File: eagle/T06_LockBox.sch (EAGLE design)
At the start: 28 parts, among them T1 2N3904, T2 2N3904, T3 2N3904

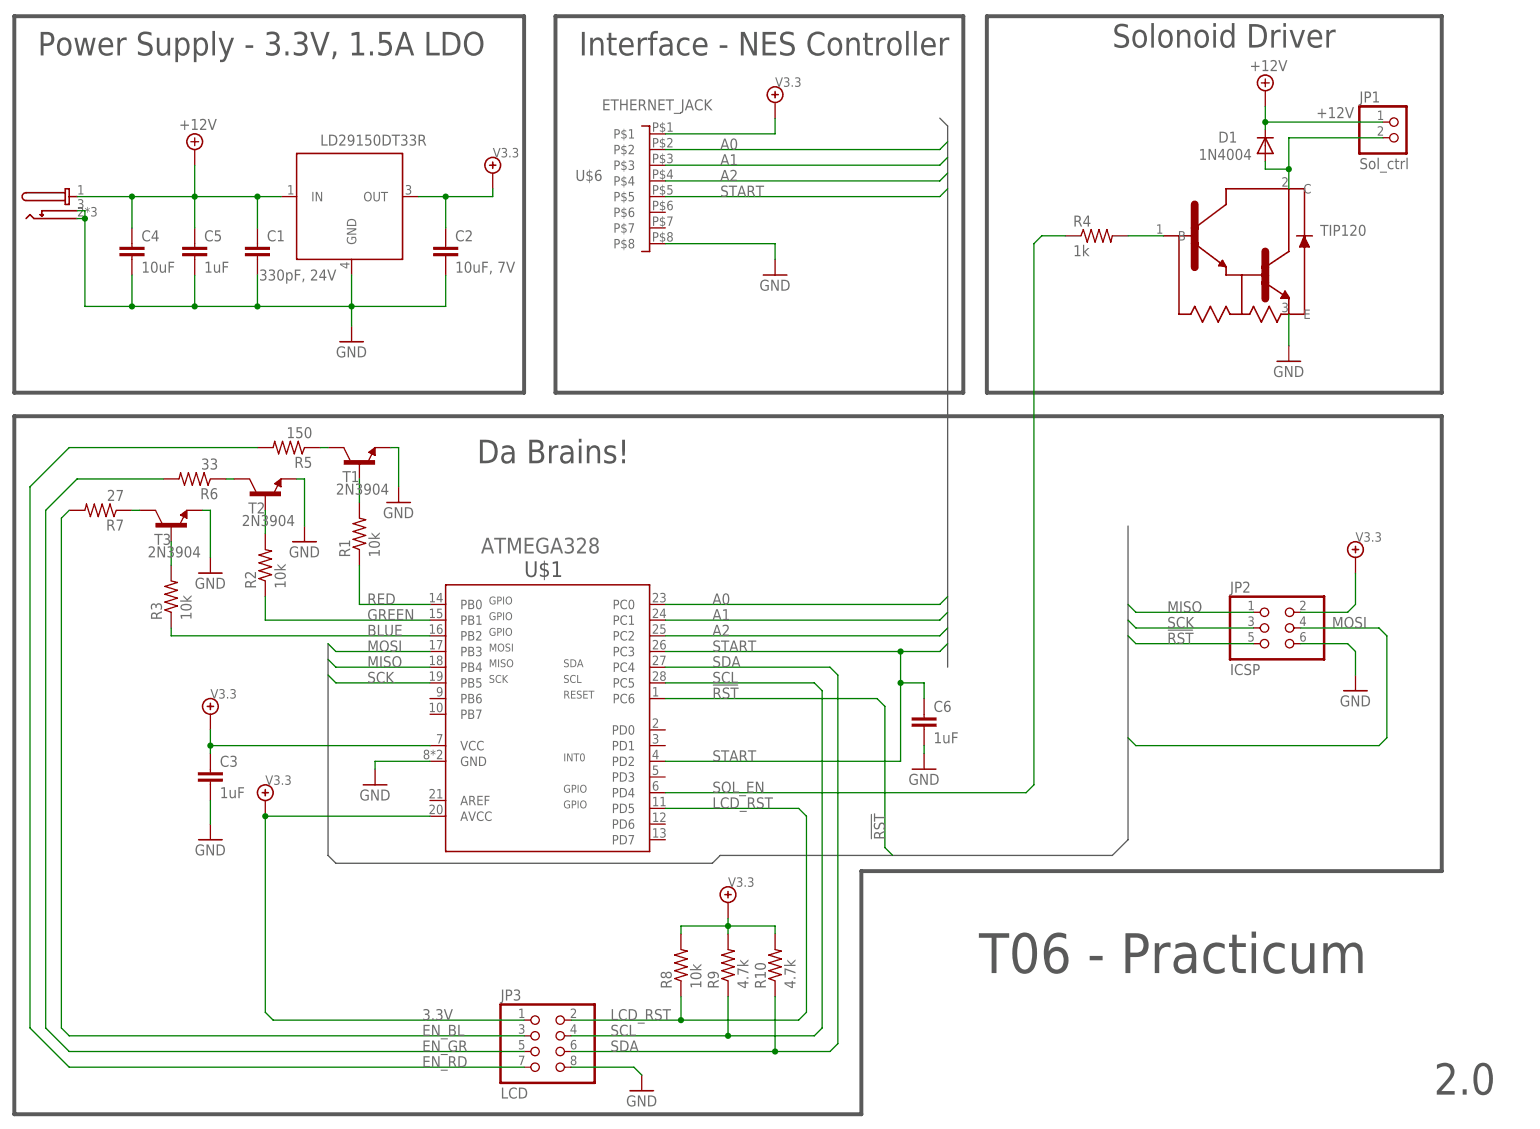
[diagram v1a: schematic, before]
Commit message: Added connections to unused pins on the schematic.  Finished routing wires to the unused pin header locaton on the board.
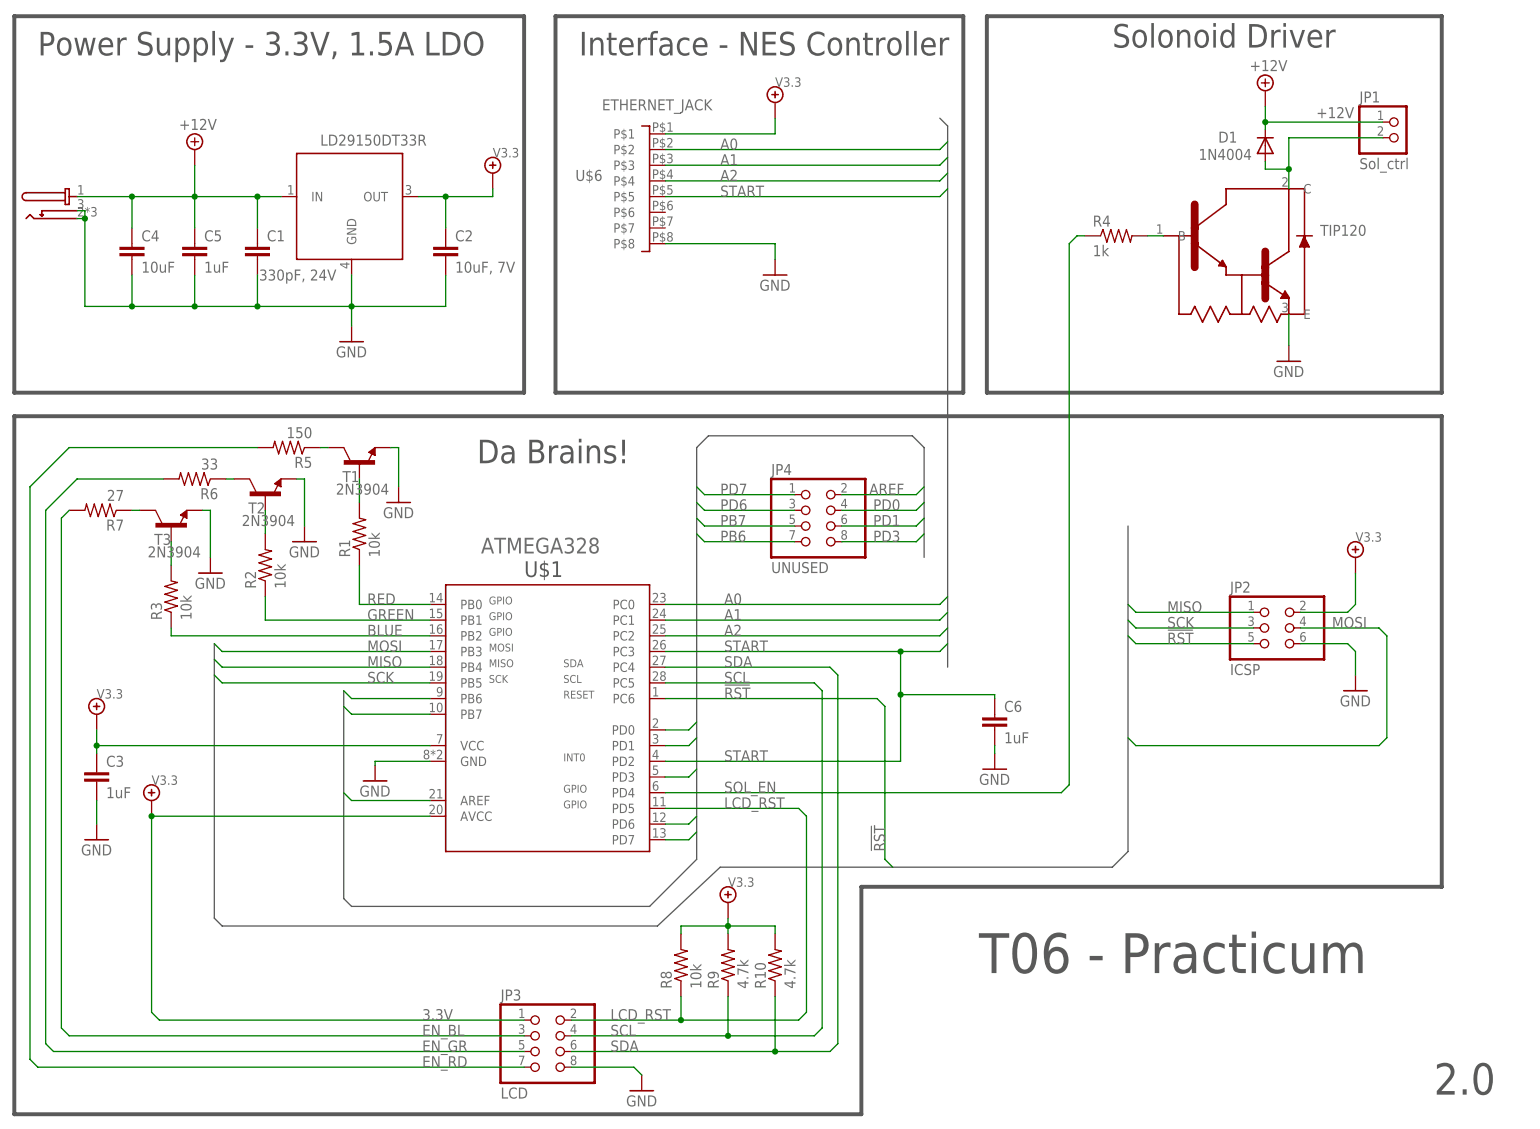
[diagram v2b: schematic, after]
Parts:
- added JP4: UNUSED, T06_Lockbox:PINHD-2X4
- C1, C2, C3, C4, C5, C6: device LockBox:C -> T06_Lockbox:C
- D1: device LockBox:1N4004 -> T06_Lockbox:1N4004
- JP1: device LockBox:PINHD-1X2 -> T06_Lockbox:PINHD-1X2
- JP2: device LockBox:PINHD-2X3 -> T06_Lockbox:PINHD-2X3
- JP3: device LockBox:PINHD-2X4 -> T06_Lockbox:PINHD-2X4
- R1, R10, R2, R3, R5, R6, R7, R8, R9: device LockBox:R-US_R0805 -> T06_Lockbox:R-US_R0805
- R4: device LockBox:R-US_M0805 -> T06_Lockbox:R-US_M0805
- T1, T2, T3: device LockBox:2N3904 -> T06_Lockbox:2N3904
- U$1: device LockBox:ATMEGA328 -> T06_Lockbox:ATMEGA328
- U$2: device LockBox:LD29150DT33R -> T06_Lockbox:LD29150DT33R
- U$3: device LockBox:PJ_075DH -> T06_Lockbox:PJ_075DH
- U$4: device LockBox:TIP120 -> T06_Lockbox:TIP120
- U$6: device LockBox:ETHERNET_JACK -> T06_Lockbox:ETHERNET_JACK
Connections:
- new net AREF: JP4.2, U$1.AREF
- new net PB6: JP4.7, U$1.PB6
- new net PB7: JP4.5, U$1.PB7
- new net PD0: JP4.4, U$1.PD0
- new net PD1: JP4.6, U$1.PD1
- new net PD3: JP4.8, U$1.PD3
- new net PD6: JP4.3, U$1.PD6
- new net PD7: JP4.1, U$1.PD7
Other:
- moved on the sheet: C3, C6, R4

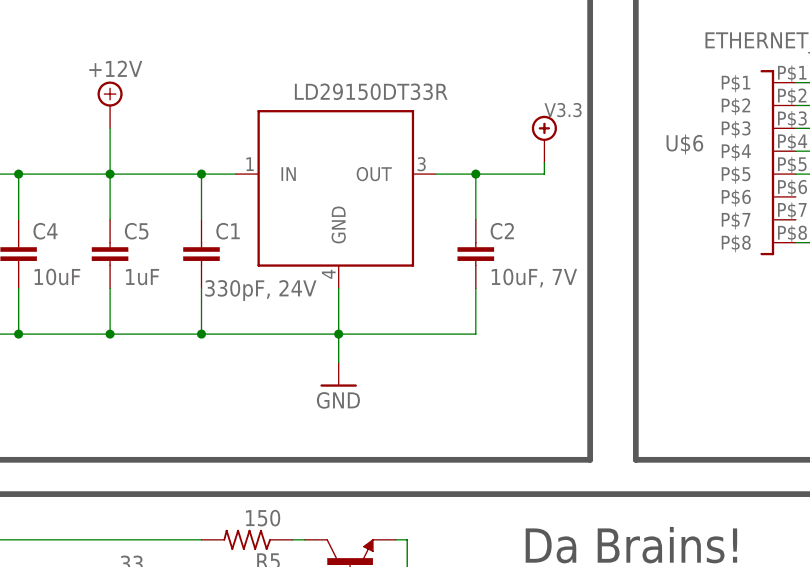
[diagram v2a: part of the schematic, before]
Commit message: Replaced 10uF 25V 0805 cap with 1206 cap.  0805 package size with those values is not available.
Moved the tplace labels of all components on the .brd
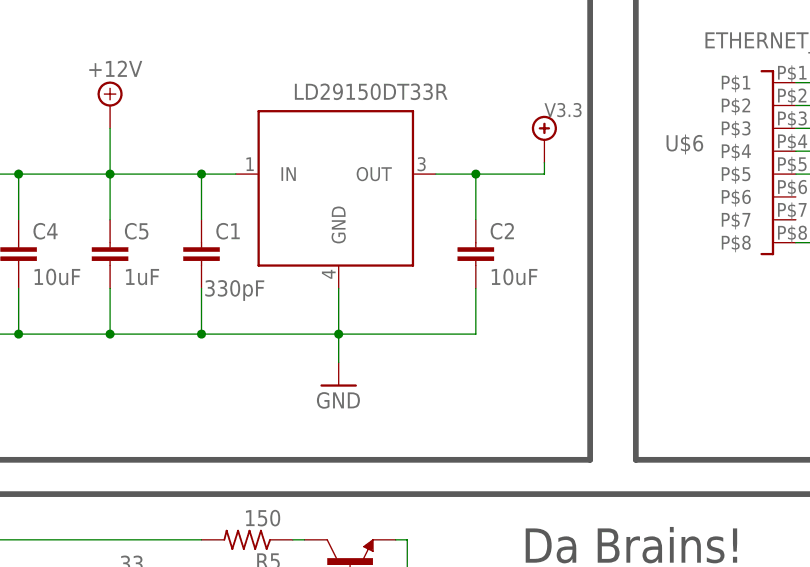
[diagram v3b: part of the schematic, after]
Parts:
- C1: value 330pF, 24V -> 330pF
- C2: value 10uF, 7V -> 10uF
- C4: device T06_Lockbox:C -> T06_Lockbox:CC1206
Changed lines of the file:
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@@
 <setting verticaltext="up"/>
 </settings>
-<grid distance="0.025" unitdist="inch" unit="inch" style="lines" multiple="1" display="yes" altdistance="0.01" altunitdist="inch" altunit="inch"/>
+<grid distance="0.1" unitdist="inch" unit="inch" style="lines" multiple="1" display="no" altdistance="0.01" altunitdist="inch" altunit="inch"/>
 <layers>
 <layer number="1" name="Top" color="4" fill="1" visible="no" active="no"/>
@@
 <part name="V4" library="T06_Lockbox" deviceset="V3.3" device=""/>
 <part name="GND5" library="T06_Lockbox" deviceset="GND" device=""/>
-<part name="C1" library="T06_Lockbox" deviceset="C" device="" value="330pF, 24V"/>
-<part name="C2" library="T06_Lockbox" deviceset="C" device="" value="10uF, 7V"/>
+<part name="C1" library="T06_Lockbox" deviceset="C" device="" value="330pF"/>
+<part name="C2" library="T06_Lockbox" deviceset="C" device="" value="10uF"/>
 <part name="R4" library="T06_Lockbox" deviceset="R-US_" device="M0805" value="1k"/>
 <part name="GND6" library="T06_Lockbox" deviceset="GND" device=""/>
@@
 <part name="R10" library="T06_Lockbox" deviceset="R-US_" device="R0805" value="4.7k"/>
 <part name="V6" library="T06_Lockbox" deviceset="V3.3" device=""/>
-<part name="C4" library="T06_Lockbox" deviceset="C" device="" value="10uF"/>
+<part name="C4" library="T06_Lockbox" deviceset="C" device="C1206" value="10uF"/>
 <part name="C5" library="T06_Lockbox" deviceset="C" device="" value="1uF"/>
 <part name="JP4" library="T06_Lockbox" deviceset="PINHD-2X4" device="" value="UNUSED"/>
